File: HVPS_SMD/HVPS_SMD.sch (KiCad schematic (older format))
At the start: 20 parts, among them J1 CONN_01X02, J2 CONN_01X02, J3 CONN_01X02, Q1 AO4294, T1 WE-FLEX_ER11_5, U1 LM3478SOIC8

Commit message: Prepare for Fab
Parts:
- removed T1: WE-FLEX_ER11_5, lib_fp:nixiemisc-WE-FLEX_ER11_5, symbol HVPS_SMD:WE-FLEX_ER11_5
- added T1: MagTop-HVSMPS, lib_fp:nixiemisc-WE-FLEX_ER11_5, symbol HVPS_SMD:MagTop-HVSMPS
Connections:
- net GND: now also T1.8
- net VCC: now also T1.5
- net at D1.A: now also T1.1
- net at Q1.5 (D), Q1.6 (D), Q1.7 (D)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: now also T1.2
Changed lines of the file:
@@
 EESchema Schematic File Version 4
-LIBS:HVPS_SMD-cache
-EELAYER 26 0
+EELAYER 30 0
 EELAYER END
 $Descr USLetter 11000 8500
@@
 $EndComp
 $Comp
-L HVPS_SMD:WE-FLEX_ER11_5 T1
-U 1 1 59C9939D
-P 6650 2000
-F 0 "T1" H 6400 2500 45  0000 L BNN
-F 1 "WE-FLEX_ER11_5" H 6400 1500 45  0000 L BNN
-F 2 "lib_fp:nixiemisc-WE-FLEX_ER11_5" H 6680 2150 20  0001 C CNN
-F 3 "" H 6650 2000 60  0001 C CNN
-	1    6650 2000
-	1    0    0    -1
-$EndComp
-$Comp
 L HVPS_SMD:MOSFET_SO08 Q1
 U 1 1 59C9950D
@@
 	6850 2100 7550 2100
 Wire Wire Line
-	6300 1600 6300 1400
-Wire Wire Line
-	6450 1600 6300 1600
-Wire Wire Line
-	6850 1800 6850 1900
-Wire Wire Line
-	7050 2200 6850 2200
-Wire Wire Line
-	7050 2550 7050 2200
-Wire Wire Line
-	6350 2550 7050 2550
-Wire Wire Line
-	6350 2400 6350 2550
-Wire Wire Line
-	6450 2400 6350 2400
-Wire Wire Line
-	6950 1600 6850 1600
-Wire Wire Line
-	6950 2400 6950 1600
-Wire Wire Line
-	6850 2400 6950 2400
-Wire Wire Line
-	6350 1800 6450 1800
-Wire Wire Line
-	6350 2200 6350 1800
-Wire Wire Line
-	6450 2200 6350 2200
-Wire Wire Line
 	5150 2850 5150 3000
 Wire Wire Line
@@
 	1    0    0    -1
 $EndComp
-Wire Wire Line
-	6300 1400 7250 1400
 Wire Wire Line
 	6450 1900 5650 1900
@@
 Wire Wire Line
 	8100 1100 8100 1400
+$Comp
+L HVPS_SMD:MagTop-HVSMPS T1
+U 1 1 5EE051E4
+P 6650 2300
+F 0 "T1" H 6653 2899 45  0000 C CNN
+F 1 "MagTop-HVSMPS" H 6653 2815 45  0000 C CNN
+F 2 "lib_fp:nixiemisc-WE-FLEX_ER11_5" H 6680 2450 20  0001 C CNN
+F 3 "" H 6650 2300 60  0001 C CNN
+	1    6650 2300
+	1    0    0    -1
+$EndComp
+Wire Wire Line
+	6850 1400 6850 1900
+Wire Wire Line
+	6850 1400 7250 1400
 $EndSCHEMATC

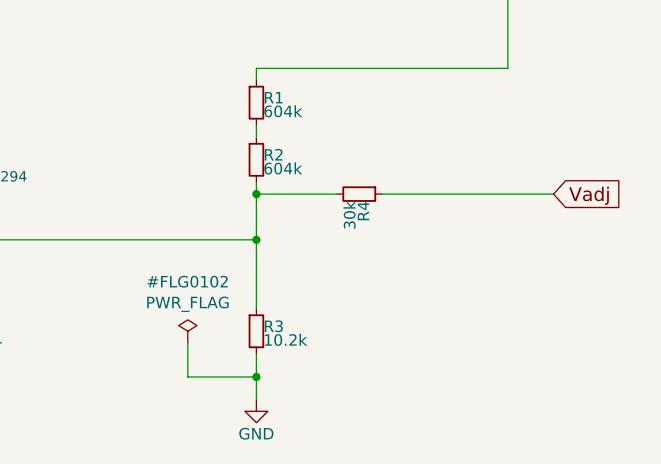
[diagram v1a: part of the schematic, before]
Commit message: Add footprint for Vfix resistor R5
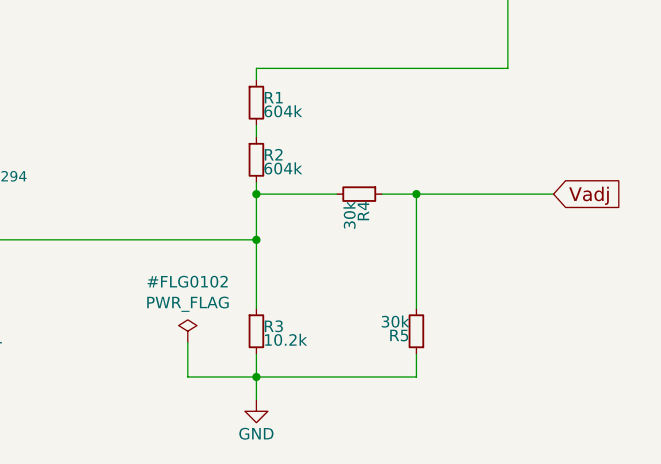
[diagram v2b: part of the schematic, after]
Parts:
- added R5: 30k, lib_fp:R_0603, symbol HVPS_SMD:R_Small
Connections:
- net GND: now also R5.1
- net Vadj: now also R5.2
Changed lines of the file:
@@
 	7000 4100 7000 4200
 Wire Wire Line
-	7550 3400 8300 3400
+	7550 3400 7700 3400
 Connection ~ 7000 3600
 Wire Wire Line
@@
 Wire Wire Line
 	6850 1400 7250 1400
+$Comp
+L HVPS_SMD:R_Small R5
+U 1 1 5EE0246C
+P 7700 4000
+F 0 "R5" H 7730 4020 50  0000 L CNN
+F 1 "30k" H 7730 3960 50  0000 L CNN
+F 2 "lib_fp:R_0603" H 7700 4000 50  0001 C CNN
+F 3 "" H 7700 4000 50  0001 C CNN
+	1    7700 4000
+	-1   0    0    1
+$EndComp
+Wire Wire Line
+	7700 3900 7700 3400
+Connection ~ 7700 3400
+Wire Wire Line
+	7700 3400 8300 3400
+Wire Wire Line
+	7700 4100 7700 4200
+Wire Wire Line
+	7700 4200 7000 4200
 $EndSCHEMATC
